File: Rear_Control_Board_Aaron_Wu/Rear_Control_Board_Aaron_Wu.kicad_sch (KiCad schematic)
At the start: 0 parts

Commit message: schematic update
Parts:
- added C1, C2, C3, C4, C5, C6, C7, C8, C9: 0.1uF,50V, SMV_Passives:Cap0805, symbol SMV_Custom:C0805C104K5RACTU
- added J1, J11, J12, J2, J3, J5, J8, J9: 430450200, SMV_Connectors:CONN_SD-43045-001_02_MOL, symbol SMV_Custom:430450200
- added J10, J7: Molex Micro-Fit 4 Pin, SMV_Connectors:4_pin0430450401, symbol SMV_Custom:Molex Micro-Fit 4 Pin
- added J4, J6: 22035035, SMV_Connectors:3pin_CON_22035035_MOL, symbol SMV_Custom:3-pin Mini Molex Spox
- added Q1, Q2, Q3, Q4: PSMN1R8-40YLC_115, LFPAK56_SOT669_NEX, symbol SMV_Custom:PSMN1R8-40YLC_115
- added R1, R2, R3, R4, R5, R6, R7, R8: R, symbol Device:R
- added U1: ~, symbol SMV_Custom:STM32_Nucleo_F446RE
- added U2: UA78M05QDCYRG4Q1, SMV_ICs:DCY4_TEX, symbol SMV_Custom:UA78M05QDCYRG4Q1
- added U3: ADS1118QDGSRQ1, DGS0010A_N, symbol SMV_Custom:ADS1118QDGSRQ1
- added U4, U5, U6: MCP6286T-E/OT, SMV_ICs:SOT-23-5_MC_MCH, symbol SMV_Custom:MCP6286T-E_OT
- added U7: MCP2562-E-P, Package_DIP:DIP-8_W7.62mm, symbol Interface_CAN_LIN:MCP2562-E-P
- added U8: ASM330LHHTR, LGA-14L_2P5X3X0P83_STM, symbol ASM330LHHTR:ASM330LHHTR
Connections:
- new net: Q1.4 (Gate), R2.1, R3.1
- new net: J3.2, J5.2, Q1.5 (Drain)
- new net: Q3.4 (Gate), R5.1, R6.2
- new net: Q4.4 (Gate), R7.2, R8.1
- new net: Q2.4 (Gate), R1.1, R4.1
- new net: J2.2, J9.2, Q2.5 (Drain)
- new net: J8.2, Q3.5 (Drain)
- new net: C9.2, U8.8 (VDD)
- new net: J1.2, Q4.5 (Drain)
- new net: J4.3, U7.6 (CANL)
- new net: J4.1, U7.7 (CANH)
- new net +12V: C2.2, C7.1, C8.1, J1.1, J10.3, J11.1, J12.1, J2.1, J3.1, J5.1, J7.3, J8.1, J9.1, U2.3 (INPUT)
- new net +3.3V: C4.1, U5.2 (VSS), U5.5 (VDD)
- new net +3V3: C3.1, C5.1, C6.1, U3.8 (VDD), U4.2 (VSS), U4.5 (VDD), U6.2 (VSS), U6.5 (VDD), U7.3 (VDD)
- new net +5V: C1.2, J6.1, U2.1 (OUTPUT)
- new net GND: C1.1, C2.1, C3.2, C4.2, C5.2, C6.2, C7.2, C8.2, J10.4, J11.2, J12.2, J4.2, J6.3, J7.4, Q1.1 (Source), Q1.2 (Source), Q1.3 (Source), Q2.1 (Source), Q2.2 (Source), Q2.3 (Source), Q3.1 (Source), Q3.2 (Source), Q3.3 (Source), Q4.1 (Source), Q4.2 (Source), Q4.3 (Source), R1.2, R2.2, R5.2, R8.2, U1.8 (GND), U2.2 (GND), U2.4 (GND), U3.3 (GND), U3.7 (AIN3), U7.2 (VSS), U7.8 (STBY), U8.7 (GND)
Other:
- note added: "AIN0"
- note added: "AIN1"
- note added: "AIN2"
- note added: "Brake light #1"
- note added: "Brake light #2"
- note added: "CAN Transceiver"
- note added: "CS_PA4"
- note added: "L turn signal"
- note added: "LDO"
- note added: "Left connector"
- note added: "MISO_PA6"
- note added: "MOSI_PA7"
- note added: "Mosfet for L turn signal"
- note added: "Mosfet for R turn signal"
- note added: "Mosfet for brake lights"
- note added: "Mosfet for tail lights"
- note added: "N"
- note added: "P"
- note added: "PA_8"
- note added: "PA_9"
- note added: "PB_6"
- note added: "PB_8"
- note added: "PB_9"
- note added: "PC_7"
- note added: "Pressure sensor"
- note added: "Q1"
- note added: "Q2"
- note added: "Q3"
- note added: "Q4"
- note added: "R turn signal"
- note added: "Right connector"
- note added: "SCLK_PA5"
- note added: "Tail light #1"
- note added: "Tail light #2"
- note added: "Torque sensor #1"
- note added: "Torque sensor #2"
- note added: "U3_CS"
- note added: "U3_MISO"
- note added: "U3_MOSI"
- note added: "U3_SCLK"
- note added: "U5"
- note added: "U6"
- note added: "U7"
- note added: "U7_RXD"
- note added: "U7_TXD"
- note added: "sensor input"

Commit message: updated rear control board
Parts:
- added C10: 0.1uF,50V, SMV_Passives:Cap0805, symbol SMV_Custom:C0805C104K5RACTU
- added R10, R9: R, symbol Device:R
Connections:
- net +3V3: now also C9.2, U8.5 (VDD_IO), U8.8 (VDD), C10.2, R10.1, R9.2
- net GND: now also C9.1, U8.6 (GND), C10.1
- net at U8.2 (RES): now also R10.2
- net at U8.3 (RES): now also R9.1
- no-connect marks 0 -> 2
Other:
- note added: "CS_PB12"
- note added: "MISO_PB14"
- note added: "MOSI_PB15"
- note added: "SCLK_PB10"
- note added: "U8_CS"
- note added: "U8_MISO"
- note added: "U8_MOSI"
- note added: "U8_SCLK"

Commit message: made feedback changes, board not done
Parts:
- added J13: 22035035, SMV_Connectors:3pin_CON_22035035_MOL, symbol SMV_Custom:3-pin Mini Molex Spox
- R1, R2, R5, R8: value R -> 100k
- R10: value R -> 10k
- R3, R4, R6, R7: value R -> 100
- R9: value R -> 33
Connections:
- net +3.3V: no longer U5.2 (VSS)
- net +3V3: now also U1.16 (+3V3); no longer U4.2 (VSS), U6.2 (VSS)
- net +5V: now also U1.18 (+5V)
- net GND: now also U1.19 (GND), U1.20 (GND), U1.22 (GND), U1.47 (GND), U1.58 (GND), U1.70 (AGND), U4.2 (VSS), U5.2 (VSS), U6.2 (VSS), J13.2; no longer U3.7 (AIN3)
- net AIN0: now reaches U5.1 (VOUT)
- net U7_RXD: now reaches U1.41 (PB8)
- net U7_TXD: now reaches U1.43 (PB9)
- net U3_SCLK: now reaches U1.49 (PA5)
- net U3_MISO: now reaches U1.51 (PA6)
- net U3_MOSI: now reaches U1.53 (PA7)
- net U8_CS: now reaches U1.54 (PB12)
- net Q3: now reaches U1.55 (PB6)
- net Q4: now reaches U1.57 (PC7)
- net Q1: now reaches U1.59 (PA9)
- net Q2: now reaches U1.61 (PA8)
- net U8_SCLK: now reaches U1.63 (PB10)
- net U8_MOSI: now reaches U1.64 (PB15)
- net U8_MISO: now reaches U1.66 (PB14)
- net AIN2: now reaches U4.1 (VOUT)
- net at U4.3 (VIN+): now also J6.2, U4.4 (VIN-)
- net PB_9: now reaches U7.1 (TXD)
- net PB_8: now reaches U7.4 (RXD)
- net AIN1: now reaches U6.1 (VOUT)
- net SCLK_PA5: now reaches U3.1 (SCLK)
- net MOSI_PA7: now reaches U3.10 (DIN)
- net CS_PA4: now reaches U3.2 (CS_N)
- net U5: now reaches U3.4 (AIN0)
- net U6: now reaches U3.5 (AIN1)
- net U7: now reaches U3.6 (AIN2)
- net MISO_PA6: now reaches U3.9 (DOUT_DRDY_N)
- net CS_PB12: now reaches U8.12 (CS)
- net SCLK_PB10: now reaches U8.13 (SCL)
- net MOSI_PB15: now reaches U8.14 (SDA)
- new net +1V0: U3.7 (AIN3)
- new net CANH net: J13.1
- new net CANL net: J13.3
- no-connect marks 2 -> 46
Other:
- note removed: "AIN0"
- note removed: "AIN1"
- note removed: "AIN2"
- note removed: "Brake light #1"
- note removed: "Brake light #2"
- note removed: "CAN Transceiver"
- note removed: "CS_PA4"
- note removed: "CS_PB12"
- note removed: "L turn signal"
- note removed: "LDO"
- note removed: "Left connector"
- note removed: "MISO_PA6"
- note removed: "MISO_PB14"
- note removed: "MOSI_PA7"
- note removed: "MOSI_PB15"
- note removed: "Mosfet for L turn signal"
- note removed: "Mosfet for R turn signal"
- note removed: "Mosfet for brake lights"
- note removed: "Mosfet for tail lights"
- note removed: "PA_8"
- note removed: "PA_9"
- note removed: "PB_6"
- note removed: "PB_8"
- note removed: "PB_9"
- note removed: "PC_7"
- note removed: "Pressure sensor"
- note removed: "Q1"
- note removed: "Q2"
- note removed: "Q3"
- note removed: "Q4"
- note removed: "R turn signal"
- note removed: "Right connector"
- note removed: "SCLK_PA5"
- note removed: "SCLK_PB10"
- note removed: "Tail light #1"
- note removed: "Tail light #2"
- note removed: "Torque sensor #1"
- note removed: "Torque sensor #2"
- note removed: "U3_CS"
- note removed: "U3_MISO"
- note removed: "U3_MOSI"
- note removed: "U3_SCLK"
- note removed: "U5"
- note removed: "U6"
- note removed: "U7"
- note removed: "U7_RXD"
- note removed: "U7_TXD"
- note removed: "U8_CS"
- note removed: "U8_MISO"
- note removed: "U8_MOSI"
- note removed: "U8_SCLK"
- note removed: "sensor input"
- moved on the sheet: C10, C4, C5, C6, C7, C8, C9, J10, J6, J7, R10, R9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

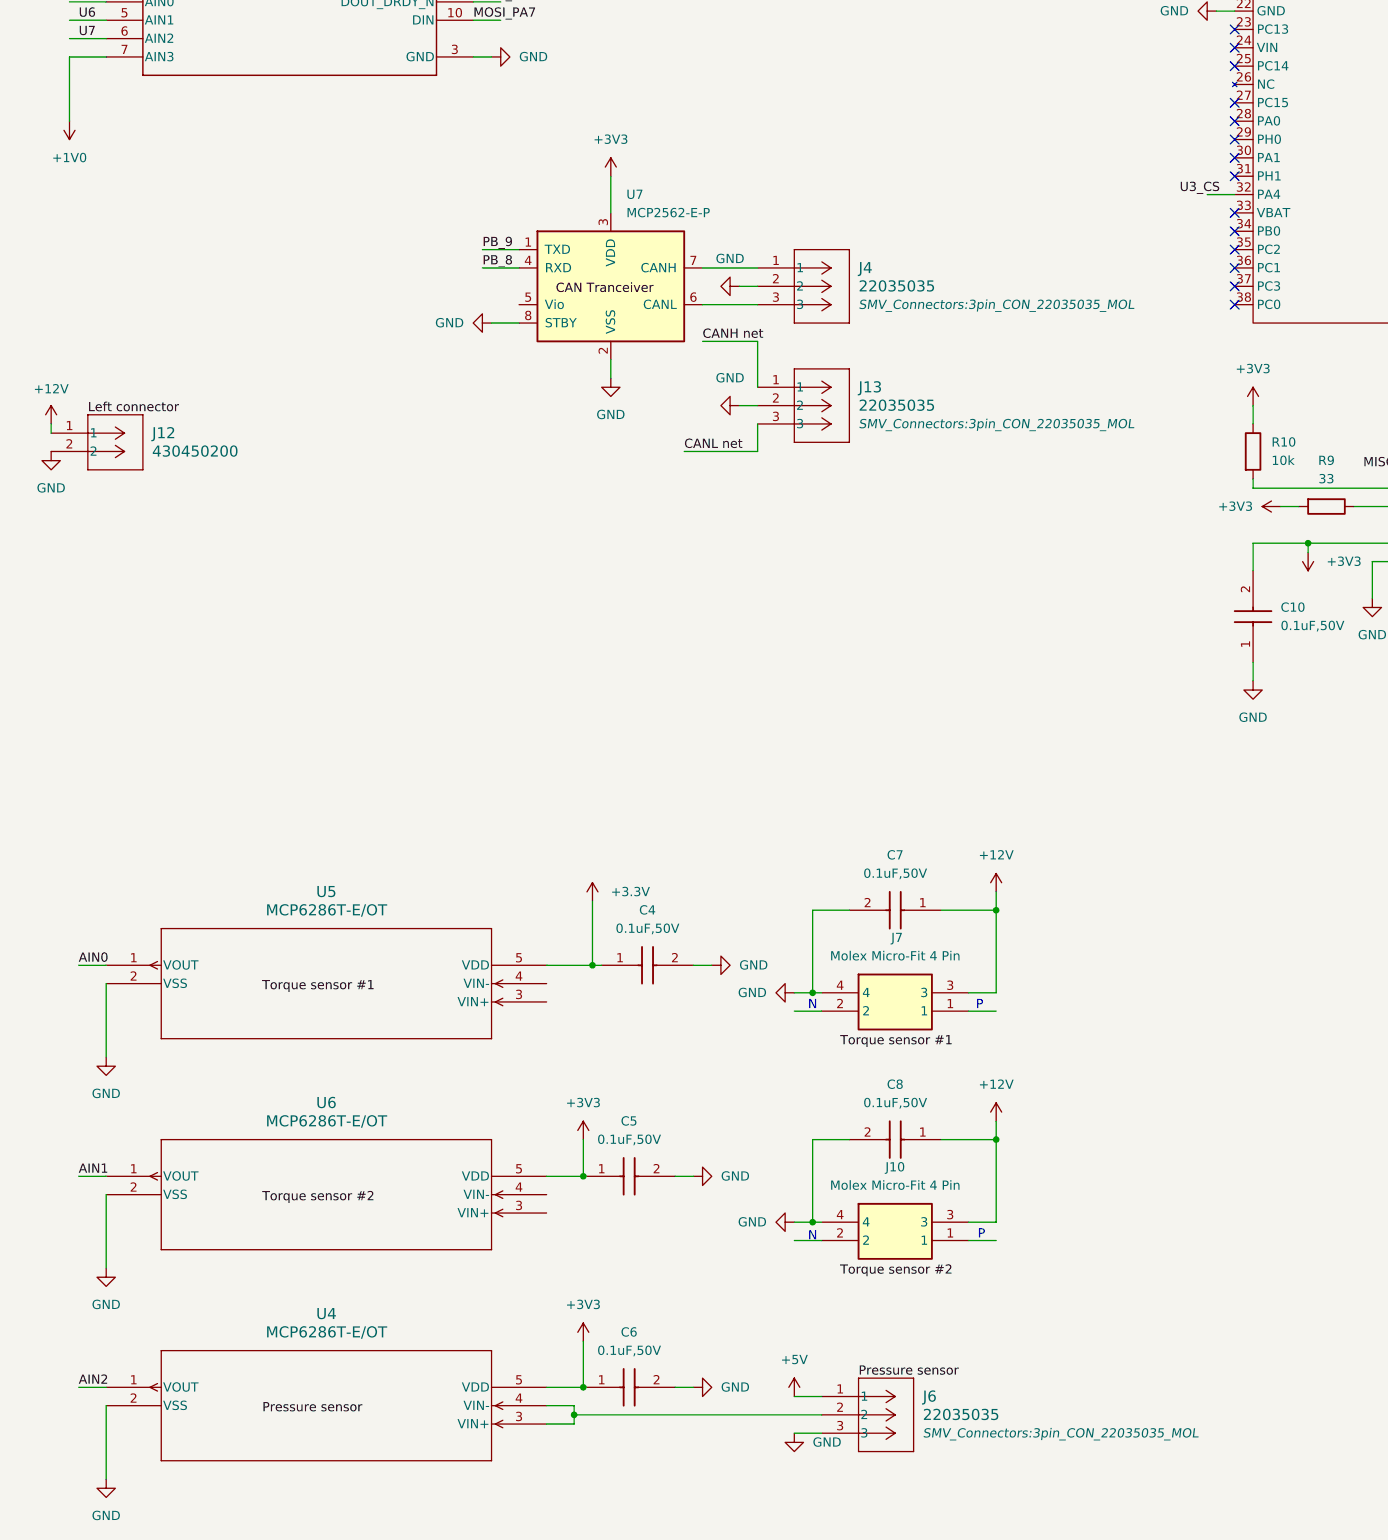
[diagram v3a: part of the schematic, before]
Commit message: schematic update, everything done but test points
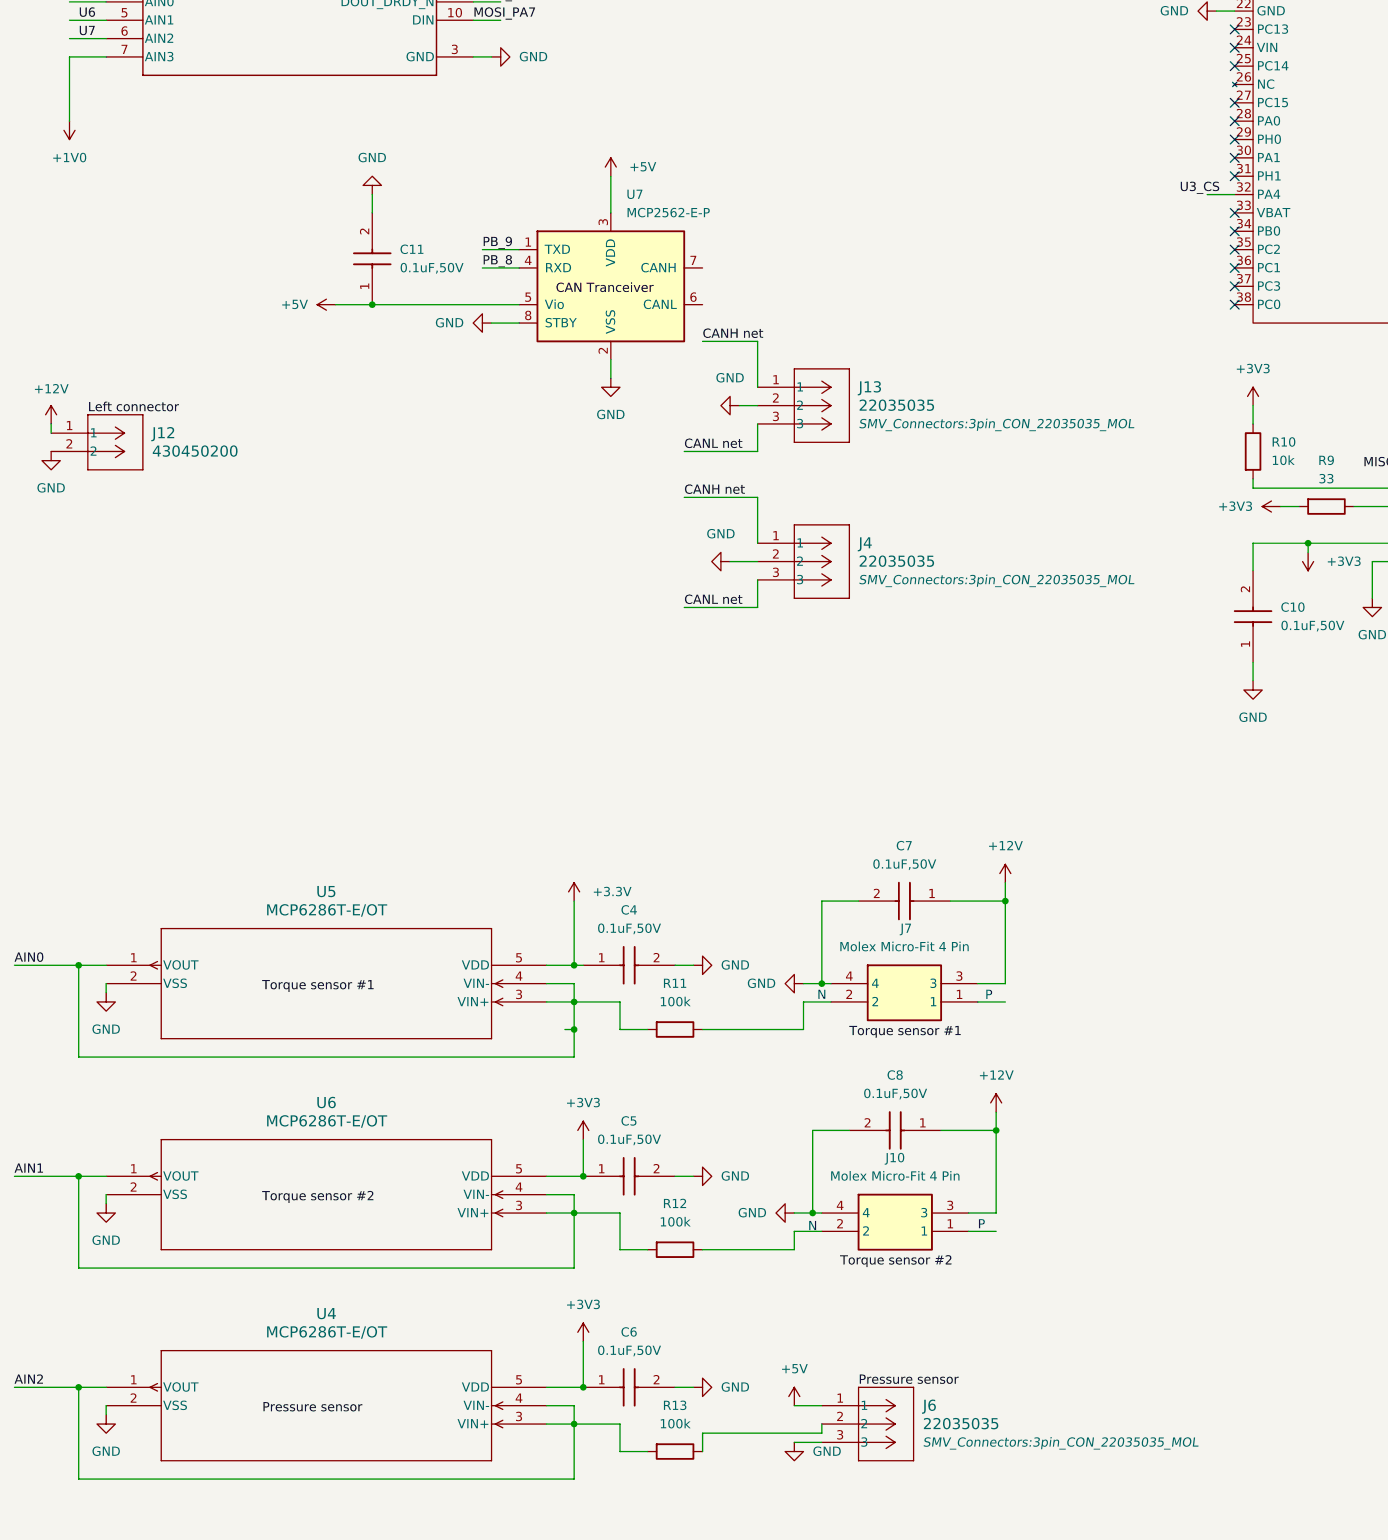
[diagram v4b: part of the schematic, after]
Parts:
- added C11: 0.1uF,50V, SMV_Passives:Cap0805, symbol SMV_Custom:C0805C104K5RACTU
- added R11, R12, R13: 100k, symbol Device:R
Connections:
- net +3V3: no longer U7.3 (VDD)
- net +5V: now also U7.3 (VDD), U7.5 (Vio), C11.1
- net AIN0: now also U5.3 (VIN+), U5.4 (VIN-), R11.2
- net AIN1: now also U6.3 (VIN+), U6.4 (VIN-), R12.2
- net AIN2: now also U4.3 (VIN+), U4.4 (VIN-), R13.2
- net CANH net: now also J4.1
- net CANL net: now also J4.3
- net GND: now also C11.2
- net at U7.6 (CANL): no longer J4.3
- net at U7.7 (CANH): no longer J4.1
- net at J7.2: now also R11.1
- net at J10.2: now also R12.1
- new net: J6.2, R13.1
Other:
- moved on the sheet: C4, C7, C8, J10, J4, J6, J7

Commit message: test points added schematic done
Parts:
- added TP1, TP10, TP11, TP12, TP13, TP14, TP15, TP16, TP17, TP18, TP19, TP2, TP20, TP21, TP22, TP23, TP24, TP25, TP26, TP27, TP28, TP29, TP3, TP30, TP31, TP32, TP33, TP34, TP35, TP36, TP37, TP38, TP39, TP4, TP40, TP41, TP42, TP43, TP44, TP45, TP46, TP47, TP48, TP49, TP5, TP50, TP51, TP52, TP53, TP54, TP55, TP56, TP57, TP58, TP59, TP6, TP60, TP61, TP62, TP63, TP7, TP8, TP9: TestPoint, symbol Connector:TestPoint
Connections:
- net +12V: now also TP42.1, TP43.1, TP49.1, TP50.1, TP51.1, TP60.1, TP62.1
- net +3.3V: now also TP36.1
- net +3V3: now also TP10.1, TP32.1, TP45.1, TP46.1, TP47.1
- net +5V: now also TP31.1, TP34.1, TP35.1, TP44.1
- net CS_PA4: now also TP55.1
- net GND: now also TP1.1, TP11.1, TP12.1, TP13.1, TP14.1, TP15.1, TP17.1, TP18.1, TP19.1, TP2.1, TP20.1, TP21.1, TP22.1, TP23.1, TP3.1, TP33.1, TP37.1, TP38.1, TP39.1, TP4.1, TP40.1, TP41.1, TP5.1, TP52.1, TP54.1, TP6.1, TP61.1, TP63.1, TP7.1, TP8.1, TP9.1
- net MISO_PA6: now also TP56.1
- net MOSI_PA7: now also TP57.1
- net PB_8: now also TP59.1
- net PB_9: now also TP58.1
- net SCLK_PA5: now also TP16.1
- net U3_SCLK: now also TP53.1
- net U8_SCLK: now also TP48.1
- net at Q1.4 (Gate), R2.1, R3.1: now also TP24.1
- net at Q3.4 (Gate), R5.1, R6.2: now also TP26.1
- net at Q4.4 (Gate), R7.2, R8.1: now also TP27.1
- net at Q2.4 (Gate), R1.1, R4.1: now also TP25.1
- net at J6.2, R13.1: now also TP30.1
- net at J10.2, R12.1: now also TP29.1
- net at J7.2, R11.1: now also TP28.1
- net +1V0 renamed +1V
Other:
- moved on the sheet: C1, C11, C2, C3, J12, J13, J4, U2, U3

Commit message: schematic done
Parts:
- removed TP15, TP17, TP33, TP37, TP38, TP40, TP41, TP48, TP52, TP54, TP61, TP63: TestPoint, symbol Connector:TestPoint
- added C12, C13, C14: 0.1uF,50V, SMV_Passives:Cap0805, symbol SMV_Custom:C0805C104K5RACTU
- added R14, R15, R16: 100k, SMV_Passives:0805RESC2012X60N, symbol Device:R
- Q1, Q2, Q3, Q4: footprint LFPAK56_SOT669_NEX -> SMV_ICs:LFPAK56_SOT669_NEX
- R1, R10, R11, R12, R13, R2, R3, R4, R5, R6, R7, R8, R9: footprint (none) -> SMV_Passives:0805RESC2012X60N
- TP1, TP10, TP11, TP12, TP13, TP14, TP16, TP18, TP19, TP2, TP20, TP21, TP22, TP23, TP24, TP25, TP26, TP27, TP28, TP29, TP3, TP30, TP31, TP32, TP34, TP35, TP36, TP39, TP4, TP42, TP43, TP44, TP45, TP46, TP47, TP49, TP5, TP50, TP51, TP53, TP55, TP56, TP57, TP58, TP59, TP6, TP60, TP62, TP7, TP8, TP9: footprint (none) -> TestPoint:TestPoint_THTPad_1.0x1.0mm_Drill0.5mm
- U1: footprint (none) -> SMV_ICs:MODULE_NUCLEO-F446RE
- U3: footprint DGS0010A_N -> SMV_ICs:DGS0010A_N
- U8: footprint LGA-14L_2P5X3X0P83_STM -> SMV_ICs:LGA-14L_2P5X3X0P83_STM
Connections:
- net CANH net is gone; now on net CAN_P net: J13.1, J4.1
- net CANL net is gone; now on net CAN_N net: J13.3, J4.3
- net MISO_PA6 is gone; now on net MISO: TP56.1, U3.9 (DOUT_DRDY_N)
- net MOSI_PB15 is gone; now on net MOSI: U8.14 (SDA)
- net SCLK_PB10 is gone; now on net SCLK: U8.13 (SCL)
- net U3_MISO is gone; now on net MISO: U1.51 (PA6)
- net U3_MOSI is gone; now on net MOSI: U1.53 (PA7)
- net U3_SCLK is gone; now on net SCLK: TP53.1, U1.49 (PA5)
- net +3.3V: now also C11.1, TP34.1, U7.5 (Vio)
- net +5V: now also U1.6 (E5V); no longer C11.1, TP34.1, U1.18 (+5V), U7.5 (Vio)
- net AIN0: now also R14.2; no longer R11.2, U5.1 (VOUT), U5.3 (VIN+), U5.4 (VIN-)
- net AIN1: now also R15.2; no longer R12.2, U6.1 (VOUT), U6.3 (VIN+), U6.4 (VIN-)
- net AIN2: now also R16.2; no longer R13.2, U4.1 (VOUT), U4.3 (VIN+), U4.4 (VIN-)
- net GND: now also C12.2, C13.2, C14.2
- net PA_8: now also R4.2
- net PA_9: now also R3.2
- net PB_6: now also R6.1
- net PC_7: now also R7.1
- net N: now reaches J10.2, R12.1, TP29.1
- net N: now also J7.2, R11.1, TP28.1
- net ADC_CS: now reaches U1.32 (PA4)
- net CAN_N net: now reaches U7.6 (CANL)
- net CAN_P net: now reaches U7.7 (CANH)
- net P: now reaches J7.1
- net P: now also J10.1
- net MISO: now reaches U8.1 (SDO/SA0)
- net MOSI_PA7 renamed MOSI
- net Q1 renamed Brake Light Mosfet
- net Q2 renamed Tail Light Mosfet
- net Q3 renamed L Turn Signal Mosfet
- net Q4 renamed R Turn Signal Mosfet
- net SCLK_PA5 renamed SCLK
- net U5 renamed Torque Sensor #1 VOUT
- net U6 renamed Torque Sensor #2 VOUT
- net U7 renamed Pressure Sensor VOUT
- net U7_RXD renamed CAN Tranceiver_RXD
- net U7_TXD renamed CAN Tranceiver_TXD
- net U8_CS renamed Accelerometer_CS
- net U8_MISO: no longer names the net of U1.66 (PB14)
- net U8_MOSI: no longer names the net of U1.64 (PB15)
- net U8_SCLK: no longer names the net of U1.63 (PB10)
- new net: C12.1, R14.1, U5.1 (VOUT), U5.4 (VIN-)
- new net: R11.2, U5.3 (VIN+)
- new net: C14.1, R16.1, U4.1 (VOUT), U4.4 (VIN-)
- new net: R13.2, U4.3 (VIN+)
- new net: R12.2, U6.3 (VIN+)
- new net: C13.1, R15.1, U6.1 (VOUT), U6.4 (VIN-)
- no-connect marks 46 -> 48
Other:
- note removed: "N"
- note removed: "P"
- moved on the sheet: C10, C3, C4, C5, C6, C7, C8, C9, J10, J13, J4, J6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
